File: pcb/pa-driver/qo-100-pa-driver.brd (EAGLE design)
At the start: 75 x 48 mm, 45 parts, among them CON1 2EDG-2P-5.08MM, Q1 BLP9G0722-20G, U1 ADP7142AUJZ, U2 2450BP15E0100

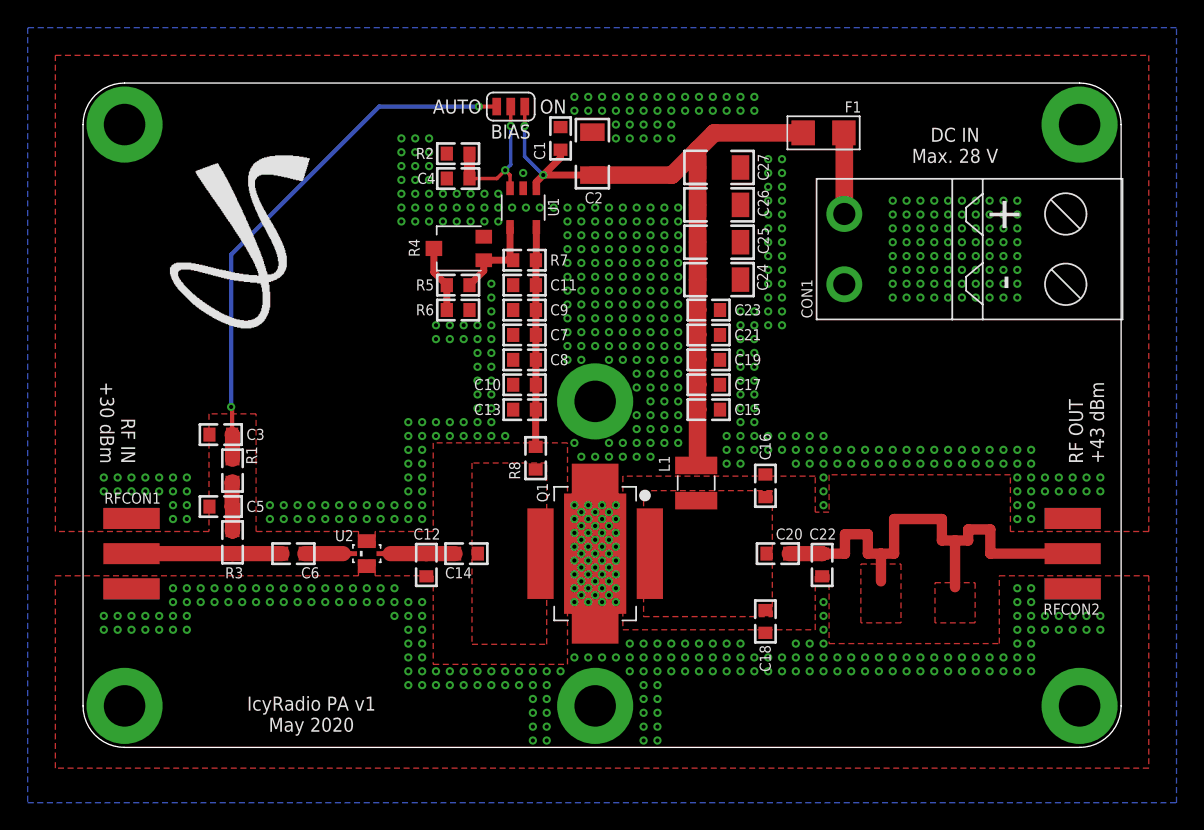
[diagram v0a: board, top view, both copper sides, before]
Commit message: New PA driver design
Signed-off-by: João Silva <jgc3silva@gmail.com>
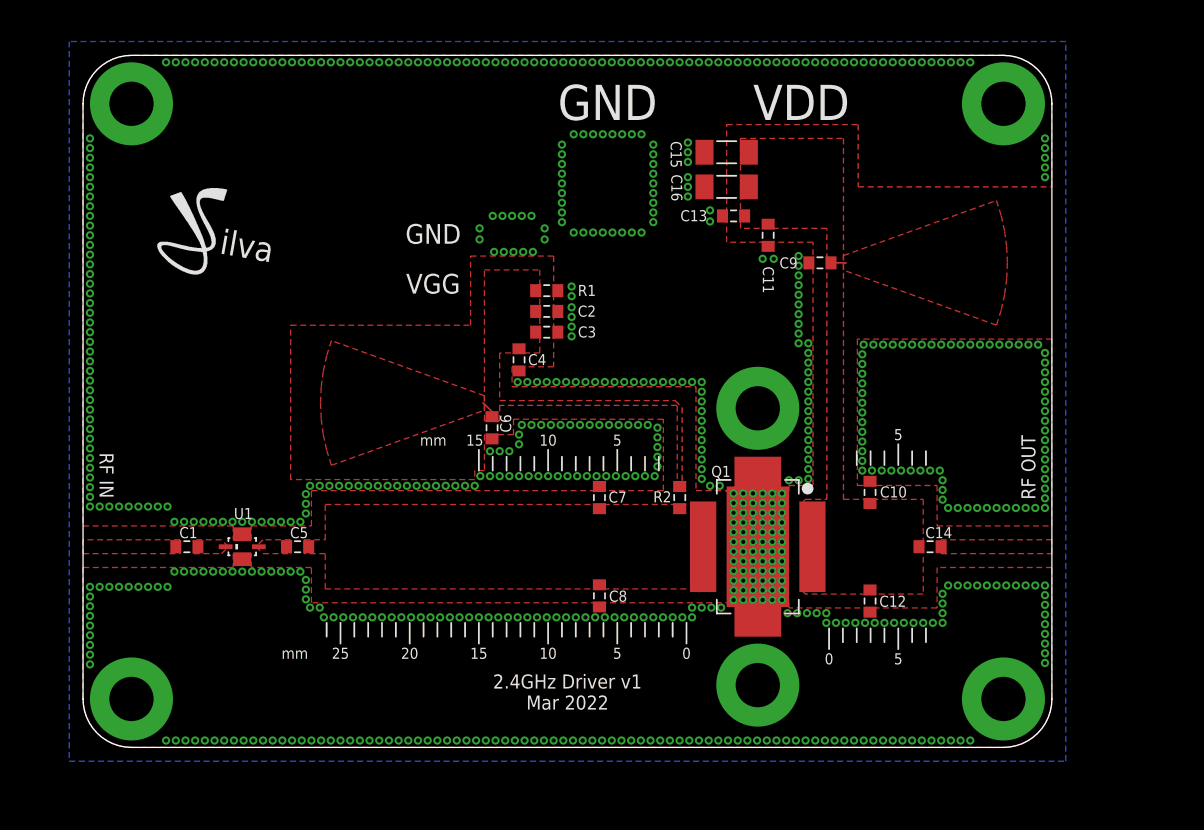
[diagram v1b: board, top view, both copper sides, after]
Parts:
- removed C17, C20: 12pF, Capacitor:CAP0603
- removed C18: 1.2pF, Capacitor:CAP0603
- removed C19: 47pF, Capacitor:CAP0603
- removed C21: 100pF, Capacitor:CAP0603
- removed C22: DNP, Capacitor:CAP0603
- removed C23: 100nF, Capacitor:CAP0603
- removed C24, C25, C26, C27: 10uF, Capacitor:CAP1206
- removed CON1: 2EDG-2P-5.08MM, Generic Connector:2EDG-2P-5.08MM
- removed F1: (no value), PTC Fuses:1206
- removed L1: 39nH, Coilcraft:1111SQ
- removed R3: 100K Ohms, Resistor:RES0603
- removed R4: 10K Ohms, Potentiometer:POT3MM
- removed R5: DNP, Resistor:RES0603
- removed R6: 3.4K Ohms, Resistor:RES0603
- removed R7: 4.7K Ohms, Resistor:RES0603
- removed R8: 5.1 Ohms, Resistor:RES0603
- removed RFCON1, RFCON2: RFCON-SMA-EDGE, RF Connector:SMA-EDGE
- removed SJ1: (no value), Solder Jumper:SJ2_S
- removed U2: 2450BP15E0100, Generic Filter:2450BP15E0100
- C1, C5: value 100nF -> 12pF
- C10: value 12pF -> 1.2pF
- C11: value 10uF -> 100pF
- C12: value 2.2pF -> 1.2pF
- C13: value 2.2pF -> 100nF
- C14: value 5.6pF -> 1.2pF
- C15: value 2.2pF -> 10uF; device Capacitor:CAP0603 -> Capacitor:CAP1206
- C16: value 0.5pF -> 10uF; device Capacitor:CAP0603 -> Capacitor:CAP1206
- C2: device Capacitor:CAP1206 -> Capacitor:CAP0603
- C4: value 100nF -> 100pF
- C6: value 12pF -> DNP
- C7: value 100pF -> 2.2pF
- C8: value 47pF -> 3.9pF
- C9: value 100nF -> DNP
- LOGO1: value JS-10MM -> JS-5MM; device Silkscreen:JS_10MM -> Silkscreen:JS_5MM
- R1: value 100K Ohms -> 10K Ohms
- R2: value 100K Ohms -> 10 Ohms
- U1: value ADP7142AUJZ -> 2450BP15E0100; device Analog Devices:SOT23-5 -> Generic Filter:2450BP15E0100
- moved C1 40.0 mm to (7.50, 14.5), turned to 0 degrees
- moved C14 33.5 mm to (61.2, 14.5)
- moved C12 32.2 mm to (56.9, 10.6)
- moved U1 31.8 mm to (11.5, 14.5), turned to 0 degrees
- moved R2 29.6 mm to (43.1, 18.1), turned to 90 degrees
- moved R1 26.2 mm to (33.5, 33.0), turned to 180 degrees
- moved C10 26.1 mm to (56.9, 18.4), turned to 90 degrees
- moved C3 24.7 mm to (33.5, 30.0), turned to 0 degrees
- moved C16 21.8 mm to (46.5, 40.5), turned to 180 degrees
- moved C9 21.6 mm to (53.2, 35.0)
- moved C13 20.6 mm to (47.0, 38.4)
- moved C15 18.6 mm to (46.5, 43.0), turned to 180 degrees
- moved C11 18.0 mm to (49.5, 37.0), turned to 270 degrees
- moved C8 17.9 mm to (37.3, 10.9), turned to 270 degrees
- moved C6 17.0 mm to (29.6, 23.1), turned to 270 degrees
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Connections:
- removed net AUTO_BIAS_EN: C3.1, R1.2, SJ1.1
- removed net BIAS_EN: C4.1, R2.2, SJ1.2, U1.3
- removed net N$1: CON1.P$2, F1.2
- removed net N$12: C6.1, R3.1, RFCON1.SIG
- removed net N$3: C16.1, C18.1, C20.1, L1.1, Q1.1
- removed net N$4: C20.2, C22.1, RFCON2.SIG
- removed net N$7: C5.1, R1.1, R3.2
- removed net N$8: R4.1, R5.2, R7.2, U1.4
- removed net N$9: R4.2, R5.1, R6.2
- new net RF_IN: C1.1
- new net RF_OUT: C14.2
- net GND: now also C6.2, R1.1, U1.1, U1.3; no longer C1.2, C17.2, C18.2, C19.2, C21.2, C22.2, C23.2, C24.2, C25.2, C26.2, C27.2, C5.2, CON1.P$1, R2.1, R6.1, RFCON1.GND@0, RFCON1.GND@1, RFCON1.GND@2, RFCON1.GND@3, RFCON2.GND@0, RFCON2.GND@1, RFCON2.GND@2, RFCON2.GND@3, U1.2, U2.1, U2.3
- net N$2: now also C5.2, C7.1, C8.1, R2.1; no longer C14.2, R8.1
- net N$5: now also C5.1, U1.2; no longer C12.1, C14.1, U2.2
- net N$6: now also C1.2, U1.4; no longer C6.2, U2.4
- net VDD: now also C10.1, C11.1, C12.1, C13.1, C14.1, C16.1, C9.1, Q1.1; no longer C1.1, C17.1, C19.1, C2.1, C21.1, C23.1, C24.1, C25.1, C26.1, C27.1, F1.1, L1.2, SJ1.3, U1.1
- net VGG: now also C2.1, C3.1, C4.1, C6.1, R1.2, R2.2; no longer C10.1, C11.1, C13.1, C7.1, C8.1, C9.1, R7.1, R8.2, U1.5
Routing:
- net VDD: track 52.1 -> 1.06 mm, vias 2 -> 0
- net AUTO_BIAS_EN: track 38.4 -> 0.00 mm, vias 2 -> 0
- net N$4: track 35.3 -> 0.00 mm
- net VGG: track 15.9 -> 1.27 mm
- net N$12: track 10.9 -> 0.00 mm
- net BIAS_EN: track 10.8 -> 0.00 mm, vias 2 -> 0
- net N$8: track 6.85 -> 0.00 mm
- net N$1: track 5.87 -> 0.00 mm
- net N$5: track 5.18 -> 0.00 mm
- net N$9: track 4.84 -> 0.00 mm
- net N$7: track 3.60 -> 0.00 mm
- net N$6: track 3.28 -> 0.00 mm
- added copper zone on layer 1, net N$5
- added copper zone on layer 1, net N$6
- added copper zone on layer 1, net RF_IN
- added copper zone on layer 1, net RF_OUT
- added copper zone on layer 1, net VDD
- added copper zone on layer 1, net VGG
- removed copper zone on layer 1, net N$3
- removed copper zone on layer 1, net N$4
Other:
- board size 75 x 48 mm -> 70 x 50 mm
- board text added: "0"
- board text added: "10"
- board text added: "15"
- board text added: "2.4GHz Driver v1 Mar 2022"
- board text added: "20"
- board text added: "25"
- board text added: "5"
- board text added: "GND"
- board text added: "RF IN"
- board text added: "RF OUT"
- board text added: "VDD"
- board text added: "VGG"
- board text added: "ilva"
- board text added: "mm"
- board text removed: "+"
- board text removed: "-"
- board text removed: "AUTO"
- board text removed: "BIAS"
- board text removed: "DC IN Max. 28 V"
- board text removed: "IcyRadio PA v1 May 2020"
- board text removed: "ON"
- board text removed: "RF IN +30 dBm"
- board text removed: "RF OUT +43 dBm"

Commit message: Add thermal sensing diode to PA Driver
Signed-off-by: João Silva <jgc3silva@gmail.com>
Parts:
- added CON1: 2P-SH-SIDE, JST:SH-02-SIDE
- added T1: 2N3904, Generic BJT:SOT23
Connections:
- new net N$1: CON1.2, T1.2
- new net N$3: CON1.1, T1.1, T1.3
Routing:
- net N$1: track 0.00 -> 7.02 mm
- net N$3: track 0.00 -> 5.34 mm
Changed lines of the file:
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@@
 <attribute name="VOLTAGE" value="" x="33.5" y="31.7" size="1.778" layer="27" display="off"/>
+</element>
+<element name="T1" library="Generic BJT" package="SOT23" value="2N3904" x="54.1" y="4.3" smashed="yes">
+<attribute name="NAME" x="53.6012" y="2.2748" size="0.8" layer="25" font="vector" ratio="10" rot="SR0" align="center-left"/>
+<attribute name="VALUE" x="50.9758" y="1.252" size="1.016" layer="27" ratio="10" rot="SR0"/>
+</element>
+<element name="CON1" library="JST" package="SH-02-SIDE" value="2P-SH-SIDE" x="58.2" y="2" smashed="yes">
+<attribute name="NAME" x="60.825" y="2.195" size="0.8" layer="25" font="vector" ratio="10" rot="R90" align="center-left"/>
+<attribute name="VALUE" x="62.645" y="0.095" size="1.27" layer="27" rot="R90"/>
 </element>
 </elements>
@@
 <signal name="S$99">
 </signal>
+<signal name="N$1">
+<contactref element="CON1" pad="2"/>
+<contactref element="T1" pad="2"/>
+<wire x1="53.0332" y1="3.3602" x2="58.2602" y2="3.3602" width="0.254" layer="1"/>
+<wire x1="58.7" y1="3.8" x2="58.7" y2="4.975" width="0.254" layer="1"/>
+<wire x1="58.2602" y1="3.3602" x2="58.7" y2="3.8" width="0.254" layer="1"/>
+</signal>
+<signal name="N$3">
+<contactref element="T1" pad="1"/>
+<contactref element="CON1" pad="1"/>
+<contactref element="T1" pad="3"/>
+<wire x1="57.7" y1="4.975" x2="57.025" y2="4.3" width="0.254" layer="1"/>
+<wire x1="57.025" y1="4.3" x2="55.1668" y2="4.3" width="0.254" layer="1"/>
+<wire x1="53.0332" y1="5.2398" x2="54.227" y2="5.2398" width="0.254" layer="1"/>
+<wire x1="54.227" y1="5.2398" x2="55.1668" y2="4.3" width="0.254" layer="1"/>
+</signal>
 </signals>
